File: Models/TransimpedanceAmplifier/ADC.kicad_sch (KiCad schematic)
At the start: 11 parts, among them U13 ADS8699

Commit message: Fixed a bug in footprint assignment
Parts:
- NT10, NT9: footprint (none) -> Connector_Custom:NetTie_0.2mm
- R19: footprint (none) -> TwoTerminal:RESC0603
- U13: footprint (none) -> IC:ADS8699
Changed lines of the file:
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@@
 			)
 		)
-		(property "Footprint" ""
+		(property "Footprint" "Connector_Custom:NetTie_0.2mm"
 			(at 81.28 109.22 0)
 			(effects
@@
 			)
 		)
-		(property "Footprint" ""
+		(property "Footprint" "IC:ADS8699"
 			(at 68.58 45.72 0)
 			(effects
@@
 			)
 		)
-		(property "Footprint" ""
+		(property "Footprint" "Connector_Custom:NetTie_0.2mm"
 			(at 81.28 152.4 0)
 			(effects
@@
 			)
 		)
-		(property "Footprint" ""
+		(property "Footprint" "TwoTerminal:RESC0603"
 			(at 164.084 62.484 90)
 			(effects

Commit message: Save progress
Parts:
- C34, C37, C38, C40: Cost $0.00 -> $0.16; Cost (qty10) (none) -> $0.090; RoHS Compliant NO -> YES
- C35, C36, C39: Cost $0.00 -> $0.14; Cost (qty10) (none) -> $0.078; RoHS Compliant NO -> YES
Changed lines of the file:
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@@
 			)
 		)
-		(property "Cost" "$0.00"
+		(property "Cost" "$0.14"
 			(at 50.8 118.11 0)
 			(effects
@@
 			)
 		)
-		(property "RoHS Compliant" "NO"
+		(property "RoHS Compliant" "YES"
+			(at 50.8 118.11 0)
+			(effects
+				(font
+					(size 1.27 1.27)
+				)
+				(hide yes)
+			)
+		)
+		(property "Cost (qty10)" "$0.078"
 			(at 50.8 118.11 0)
 			(effects
@@
 			)
 		)
-		(property "Cost" "$0.00"
+		(property "Cost" "$0.14"
 			(at 132.08 118.11 0)
 			(effects
@@
 			)
 		)
-		(property "RoHS Compliant" "NO"
+		(property "RoHS Compliant" "YES"
+			(at 132.08 118.11 0)
+			(effects
+				(font
+					(size 1.27 1.27)
+				)
+				(hide yes)
+			)
+		)
+		(property "Cost (qty10)" "$0.078"
 			(at 132.08 118.11 0)
 			(effects
@@
 			)
 		)
-		(property "Cost" "$0.00"
+		(property "Cost" "$0.16"
 			(at 73.66 161.29 0)
 			(effects
@@
 			)
 		)
-		(property "RoHS Compliant" "NO"
+		(property "RoHS Compliant" "YES"
+			(at 73.66 161.29 0)
+			(effects
+				(font
+					(size 1.27 1.27)
+				)
+				(hide yes)
+			)
+		)
+		(property "Cost (qty10)" "$0.090"
 			(at 73.66 161.29 0)
 			(effects
@@
 			)
 		)
-		(property "Cost" "$0.00"
+		(property "Cost" "$0.14"
 			(at 50.8 161.29 0)
 			(effects
@@
 			)
 		)
-		(property "RoHS Compliant" "NO"
+		(property "RoHS Compliant" "YES"
+			(at 50.8 161.29 0)
+			(effects
+				(font
+					(size 1.27 1.27)
+				)
+				(hide yes)
+			)
+		)
+		(property "Cost (qty10)" "$0.078"
 			(at 50.8 161.29 0)
 			(effects
@@
 			)
 		)
-		(property "Cost" "$0.00"
+		(property "Cost" "$0.16"
 			(at 73.66 118.11 0)
 			(effects
@@
 			)
 		)
-		(property "RoHS Compliant" "NO"
+		(property "RoHS Compliant" "YES"
+			(at 73.66 118.11 0)
+			(effects
+				(font
+					(size 1.27 1.27)
+				)
+				(hide yes)
+			)
+		)
+		(property "Cost (qty10)" "$0.090"
 			(at 73.66 118.11 0)
 			(effects
@@
 			)
 		)
-		(property "Cost" "$0.00"
+		(property "Cost" "$0.16"
 			(at 30.48 64.77 0)
 			(effects
@@
 			)
 		)
-		(property "RoHS Compliant" "NO"
+		(property "RoHS Compliant" "YES"
+			(at 30.48 64.77 0)
+			(effects
+				(font
+					(size 1.27 1.27)
+				)
+				(hide yes)
+			)
+		)
+		(property "Cost (qty10)" "$0.090"
 			(at 30.48 64.77 0)
 			(effects
@@
 			)
 		)
-		(property "Cost" "$0.00"
+		(property "Cost" "$0.16"
 			(at 154.94 118.11 0)
 			(effects
@@
 			)
 		)
-		(property "RoHS Compliant" "NO"
+		(property "RoHS Compliant" "YES"
 			(at 154.94 118.11 0)
 			(effects
+				(font
+					(size 1.27 1.27)
+				)
+				(hide yes)
+			)
+		)
+		(property "Cost (qty10)" "$0.090"
+			(at 154.94 118.11 0)
+			(effects

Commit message: Almost done with generating bill of materials
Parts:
- NT10, NT9: Cost $0.00 -> (none); RoHS Compliant NO -> (none)
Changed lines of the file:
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@@
 			)
 		)
-		(property "Cost" "$0.00"
+		(property "Cost" ""
 			(at 81.28 109.22 0)
 			(effects
@@
 			)
 		)
-		(property "RoHS Compliant" "NO"
+		(property "RoHS Compliant" ""
 			(at 81.28 109.22 0)
 			(effects
@@
 			)
 		)
-		(property "Cost" "$0.00"
+		(property "Cost" ""
 			(at 81.28 152.4 0)
 			(effects
@@
 			)
 		)
-		(property "RoHS Compliant" "NO"
+		(property "RoHS Compliant" ""
 			(at 81.28 152.4 0)
 			(effects

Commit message: Going to shift all the expensive, hard-to-find ICs over to Mouser
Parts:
- R19: Cost $0.00 -> $0.10; Cost (qty10) (none) -> $0.030; RoHS Compliant NO -> YES
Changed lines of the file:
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@@
 			)
 		)
-		(property "Cost" "$0.00"
+		(property "Cost" "$0.10"
 			(at 163.83 63.5 90)
 			(effects
@@
 			)
 		)
-		(property "RoHS Compliant" "NO"
+		(property "RoHS Compliant" "YES"
 			(at 163.83 63.5 90)
 			(effects
+				(font
+					(size 1.27 1.27)
+				)
+				(hide yes)
+			)
+		)
+		(property "Cost (qty10)" "$0.030"
+			(at 163.83 63.5 90)
+			(effects

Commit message: Exclude these pin headers from the BOM; they are just cheap breakaway pins
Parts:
- U13: Cost $0.00 -> $8.57; Cost (qty10) (none) -> $6.648; RoHS Compliant NO -> YES
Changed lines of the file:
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@@
 			)
 		)
-		(property "Cost" "$0.00"
+		(property "Cost" "$8.57"
 			(at 68.58 45.72 0)
 			(effects
@@
 			)
 		)
-		(property "RoHS Compliant" "NO"
+		(property "RoHS Compliant" "YES"
 			(at 68.58 45.72 0)
 			(effects
+				(font
+					(size 1.27 1.27)
+				)
+				(hide yes)
+			)
+		)
+		(property "Cost (qty10)" "$6.648"
+			(at 68.58 45.72 0)
+			(effects

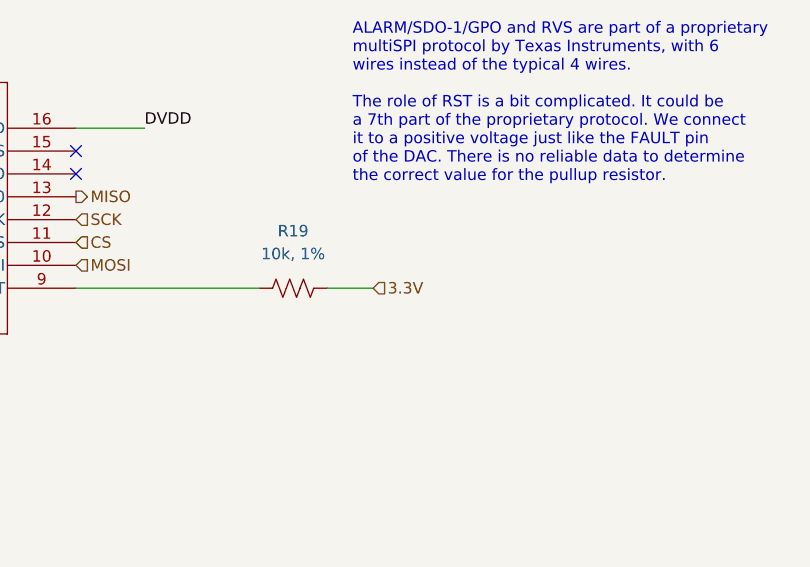
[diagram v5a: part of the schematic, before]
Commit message: Removed some complexity from the schematic while solving the layout problem
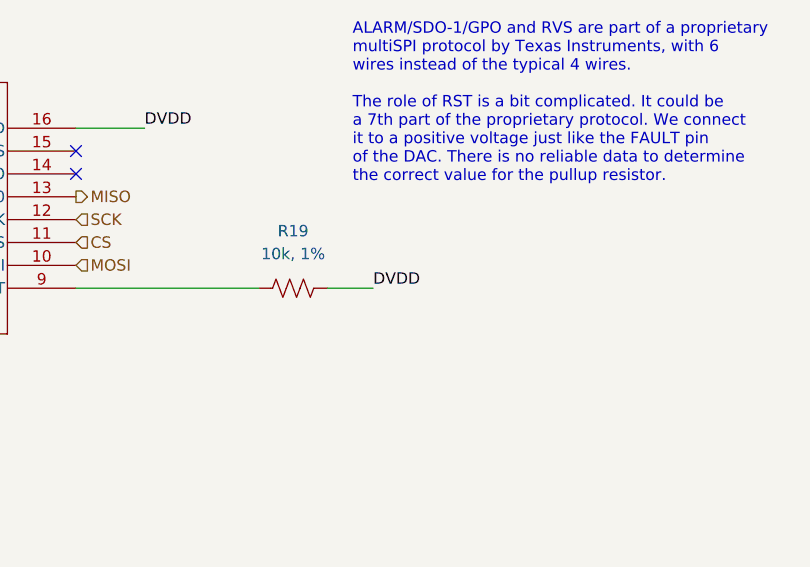
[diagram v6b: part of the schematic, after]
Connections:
- net 3.3V: no longer R19.2
- net DVDD: now also R19.2
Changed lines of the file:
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@@
+		)
+	)
+	(label "DVDD"
+		(at 172.72 63.5 0)
+		(effects
+			(font
+				(size 1.27 1.27)
+			)
+			(justify left bottom)
 		)
 	)
@@
 		(effects
 			(font
-				(size 1.27 1.27)
-			)
-			(justify left)
-		)
-	)
-	(hierarchical_label "3.3V"
-		(shape input)
-		(at 172.72 63.5 0)
-		(effects
-			(font
